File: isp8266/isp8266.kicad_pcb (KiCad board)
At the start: 2 copper layers, 60 x 35 mm, 68 parts, among them J1 Bottom, J10 BAT2, J11 USB_C_Receptacle_USB2.0, J12 F1, J2 Up, J7 F0, J8 BAT1, Q1 S8050, Q2 S8050, Q3 BSS138, Q4 IRLML6402, Q5 BSS138, Q6 IRLML6402, U1 CH340C, U2 AP1117-33, U3 IP5306, U4 ESP-07

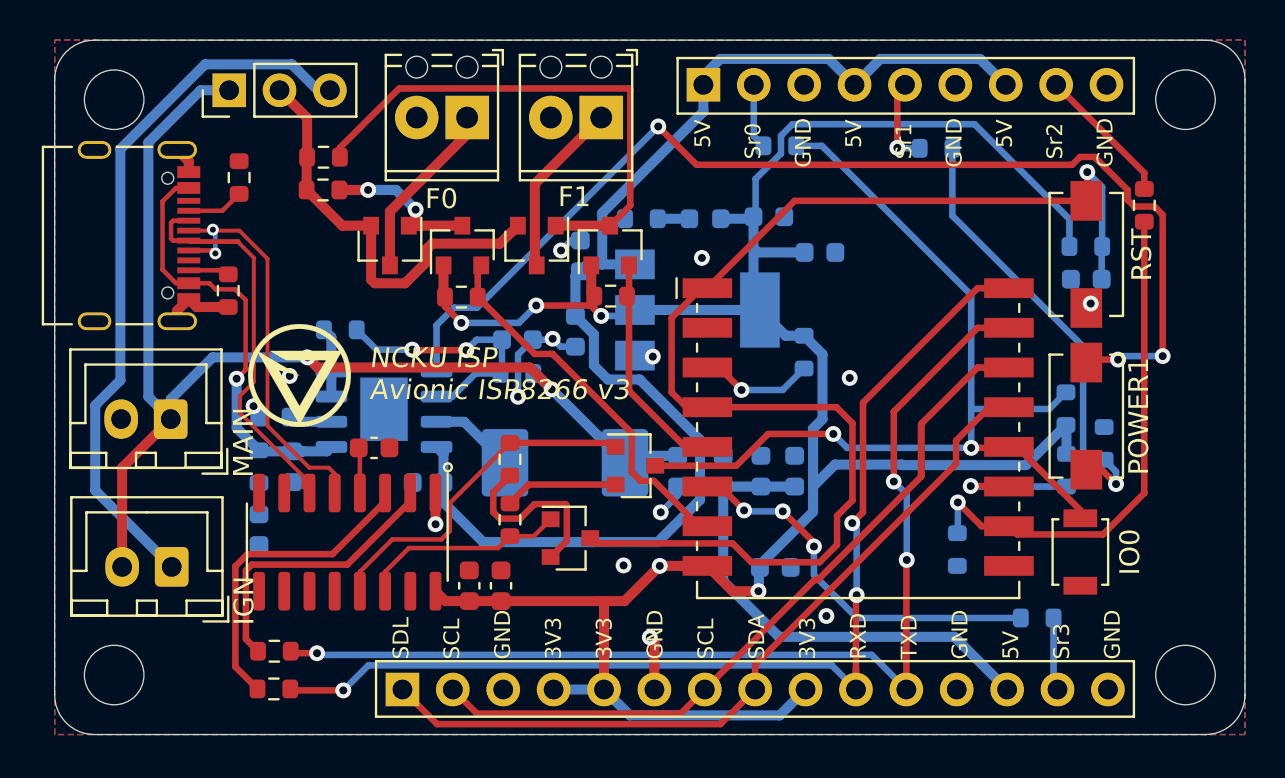
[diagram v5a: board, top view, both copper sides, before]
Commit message: Use kicad and panelized
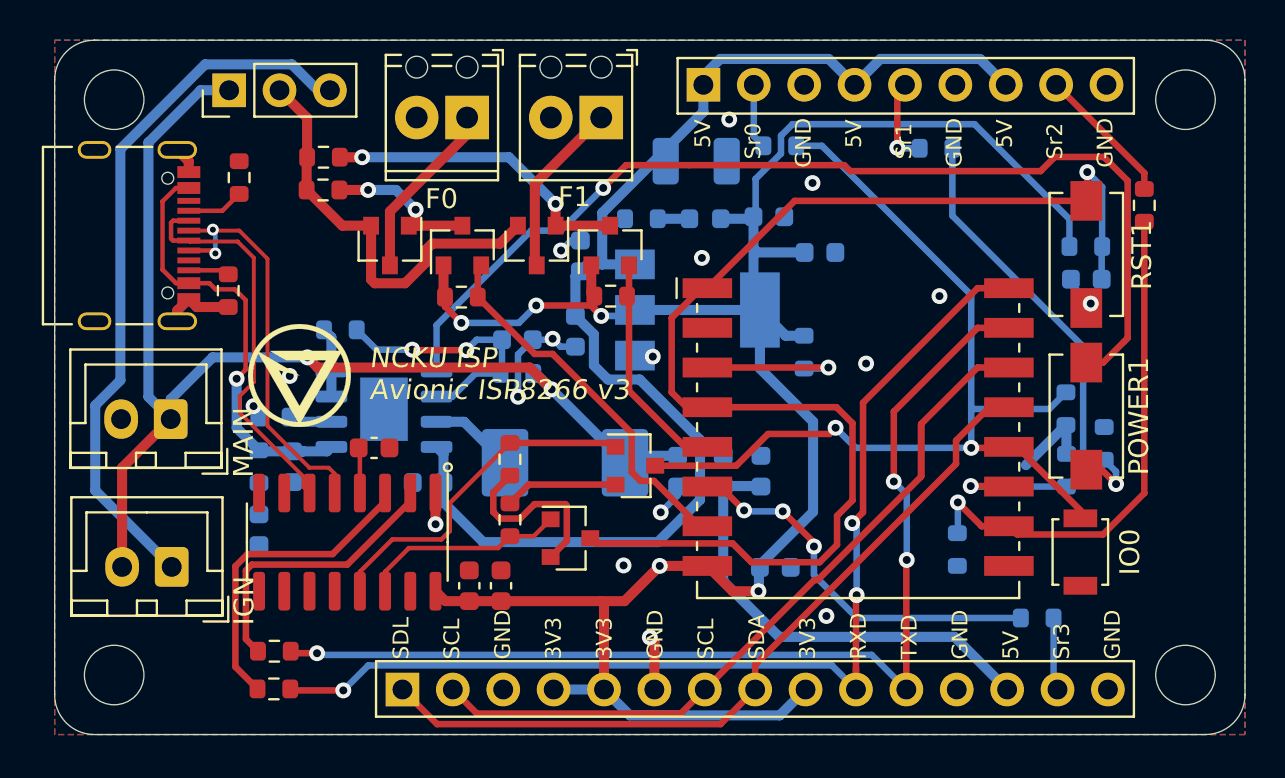
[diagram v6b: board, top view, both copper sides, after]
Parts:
- C14: value 22u -> 220u; footprint Capacitor_SMD:C_0603_1608Metric -> Capacitor_Tantalum_SMD:CP_EIA-3528-12_Kemet-T
- moved C14 16.4 mm to (69.3, 26.6), turned to 0 degrees
- renumbered RST to RST1
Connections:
- J11 pad A8: Net-(J11-PadA8) -> unconnected-(J11-PadA8)
- J11 pad B8: Net-(J11-PadB8) -> unconnected-(J11-PadB8)
- U1 pad 10: Net-(U1-Pad10) -> unconnected-(U1-Pad10)
- U1 pad 11: Net-(U1-Pad11) -> unconnected-(U1-Pad11)
- U1 pad 12: Net-(U1-Pad12) -> unconnected-(U1-Pad12)
- U1 pad 15: Net-(U1-Pad15) -> unconnected-(U1-Pad15)
- U1 pad 7: Net-(U1-Pad7) -> unconnected-(U1-Pad7)
- U1 pad 8: Net-(U1-Pad8) -> unconnected-(U1-Pad8)
- U1 pad 9: Net-(U1-Pad9) -> unconnected-(U1-Pad9)
- U4 pad 2: Net-(U4-Pad2) -> unconnected-(U4-Pad2)
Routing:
- net Net-(Q4-Pad1): track 26.4 -> 15.7 mm, vias 0 -> 2
- net +3V3: track 122.8 -> 113.4 mm
- net Net-(POWER1-Pad1): track 56.7 -> 51.9 mm, vias 3 -> 1
- net +5V: track 90.6 -> 87.9 mm
- net D-: track 22.5 -> 20.0 mm
- net EN: track 5.80 -> 7.35 mm
- net -BATT: vias 14 -> 17
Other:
- net class Default removed
